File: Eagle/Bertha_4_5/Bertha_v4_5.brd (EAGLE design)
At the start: 100 x 83.6 mm, 132 parts, among them CON1 JACK_DC_BARREL, CON2 JACK_DC_BARREL, IC1 MCP1703DB, IC4 DRV8811, J1 RJ12RIGHTANGLE-I2C, J2 RJ12RIGHTANGLE-I2C, Q5 BSP75, Q6 BSP75, U1 HX711, U100 RN2483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

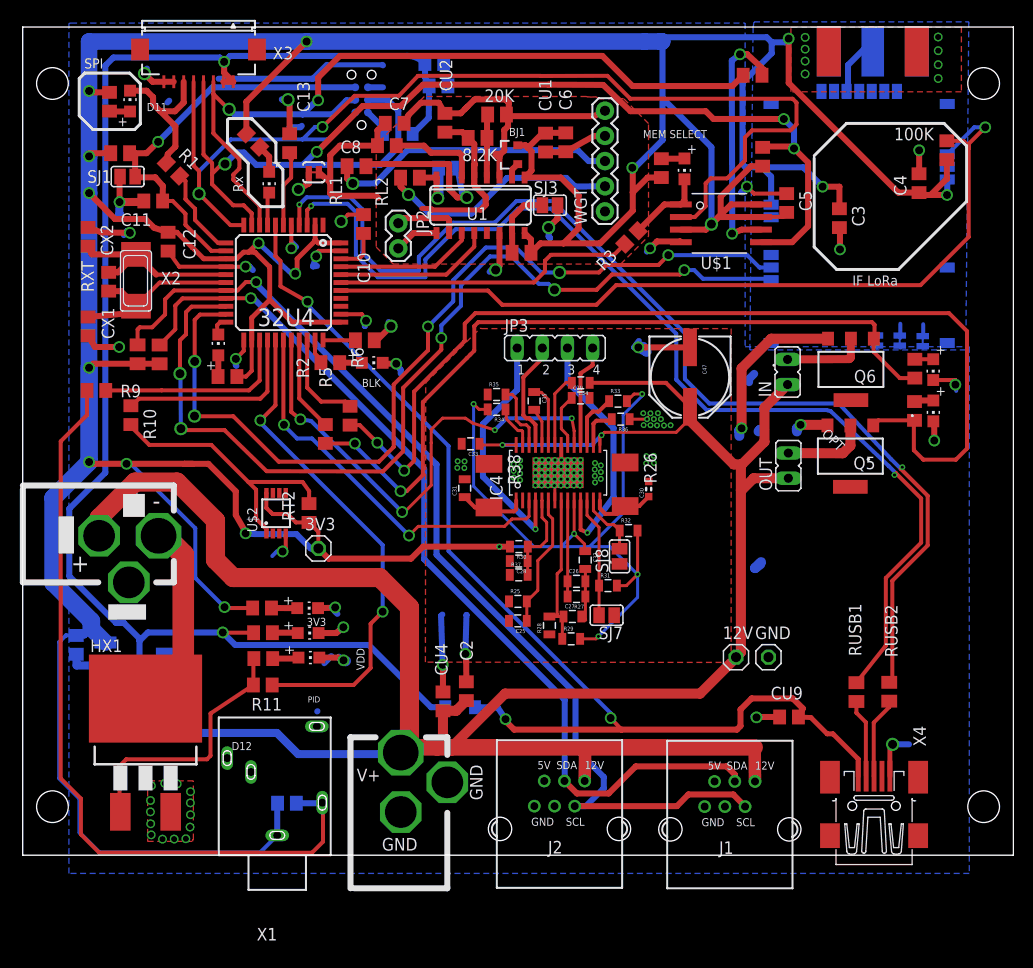
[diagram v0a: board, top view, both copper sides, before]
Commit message: correted PID diode, 4.5 finished, closes #72, ref #47
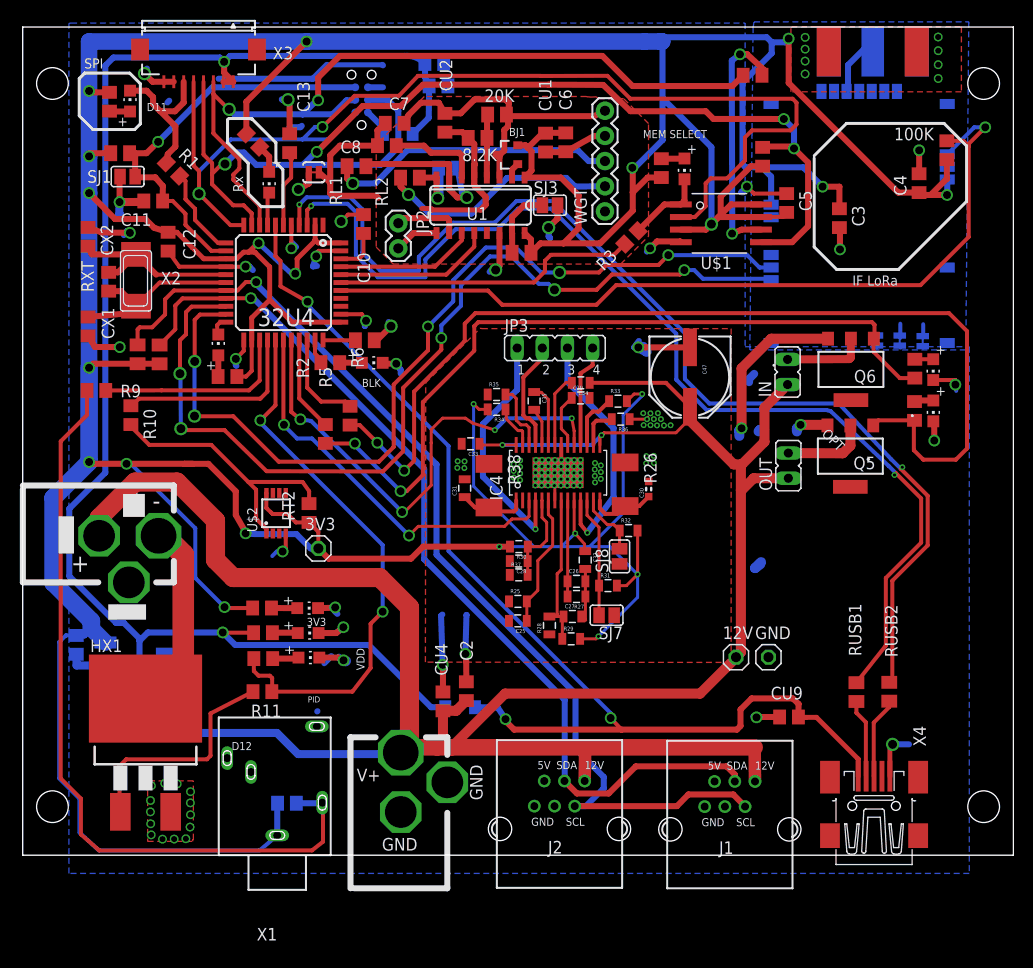
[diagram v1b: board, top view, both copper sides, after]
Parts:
- HX1: value IPB081N06L3GATMA1 -> 3v3 IGBT
- R28: value 0R -> Rlim
- moved R11 0.67 mm to (19.2, 14.6)
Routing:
- net D6*: track 50.0 -> 55.3 mm
- net N$6: track 26.4 -> 23.4 mm

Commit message: corrected powerFET labelling
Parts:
- HX1: value 3v3 IGBT -> <3V th / 10A
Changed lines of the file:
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@@
 </element>
 <element name="RK1" library="resistor" package="M0805" value="10K" x="8.82023125" y="48.6536625" smashed="yes" rot="R90"/>
-<element name="HX1" library="transistor-power" package="D2PACK" value="3v3 IGBT" x="7.39551875" y="11.3685"/>
+<element name="HX1" library="transistor-power" package="D2PACK" value="&lt;3V th / 10A" x="7.39551875" y="11.3685" smashed="yes">
+<attribute name="NAME" x="1.80751875" y="18.6075" size="1.27" layer="25"/>
+<attribute name="VALUE" x="3.2" y="7.980075" size="0.8128" layer="27"/>
+</element>
 <element name="R11" library="rcl" package="R0805" value="1K" x="19.194778125" y="14.6140875" smashed="yes" rot="R180">
 <attribute name="NAME" x="21.128021875" y="13.305246875" size="1.27" layer="25" rot="R180"/>

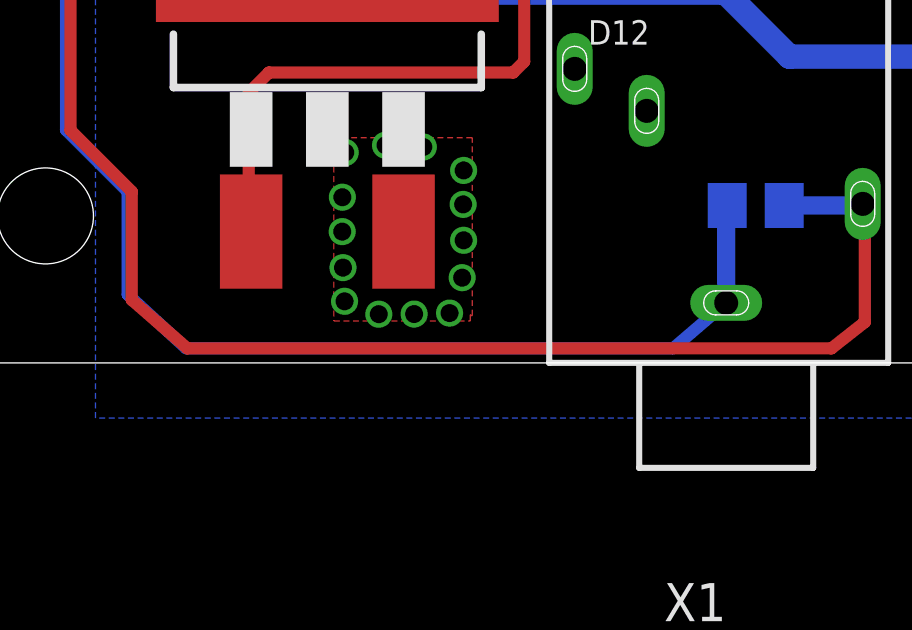
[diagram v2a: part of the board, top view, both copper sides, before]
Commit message: added protection resistor, closes #74
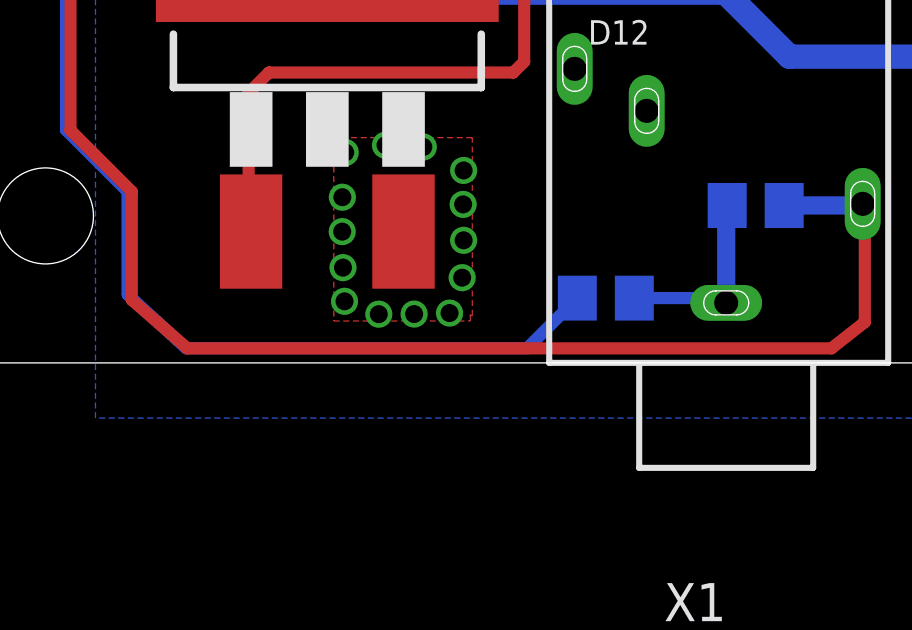
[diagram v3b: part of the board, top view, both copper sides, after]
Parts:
- added R4: 100, rcl:R0805
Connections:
- new net N$14: R4.1, RT1.1, X1.1
- net 3.3V: now also R4.2; no longer RT1.1, X1.1
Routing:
- net 3.3V: track 583.8 -> 575.7 mm
- net N$14: track 0.00 -> 6.39 mm
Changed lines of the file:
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@@
 </element>
 <element name="JP3" library="jumper" package="JP4" value="" x="48.7194" y="49.297871875"/>
+<element name="R4" library="rcl" package="R0805" value="100" x="16.678528125" y="0.2596125" smashed="yes" rot="MR0">
+<attribute name="NAME" x="17.313528125" y="1.5296125" size="1.27" layer="26" rot="MR0"/>
+<attribute name="VALUE" x="18.344796875" y="1.675675" size="1.27" layer="28" rot="MR0"/>
+</element>
 </elements>
 <signals>
@@
 <wire x1="47.592296875" y1="71.108425" x2="45.998725" y2="69.514853125" width="0.6096" layer="1"/>
 <contactref element="RT2" pad="1"/>
-<contactref element="RT1" pad="1"/>
 <contactref element="RK15" pad="1"/>
 <contactref element="RK16" pad="1"/>
@@
 <wire x1="58.084196875" y1="66.5093625" x2="56.578546875" y2="65.0037125" width="0.6096" layer="1"/>
 <wire x1="56.578546875" y1="65.0037125" x2="56.578546875" y2="63.1641625" width="0.6096" layer="1"/>
-<contactref element="X1" pad="1"/>
 <contactref element="U$2" pad="8"/>
 <wire x1="20.0952625" y1="32.67880625" x2="19.589753125" y2="33.144575" width="0.4064" layer="1"/>
@@
 <wire x1="22.625440625" y1="30.51745" x2="24.075609375" y2="29.06728125" width="0.6096" layer="16"/>
 <wire x1="24.075609375" y1="29.06728125" x2="24.84389375" y2="29.06728125" width="0.6096" layer="16"/>
-<wire x1="20.724303125" y1="3.347709375" x2="20.691253125" y2="3.314659375" width="0.6096" layer="16"/>
-<wire x1="20.691253125" y1="3.314659375" x2="20.691253125" y2="0.101475" width="0.6096" layer="16"/>
 <wire x1="-1.314634375" y1="5.865509375" x2="0.741525" y2="3.80935" width="0.4064" layer="16"/>
 <wire x1="0.741525" y1="3.80935" x2="0.741525" y2="0.3821125" width="0.4064" layer="16"/>
 <wire x1="0.741525" y1="0.3821125" x2="2.68780625" y2="-1.4120125" width="0.4064" layer="16"/>
-<wire x1="2.68780625" y1="-1.4120125" x2="18.924171875" y2="-1.4120125" width="0.4064" layer="16"/>
-<wire x1="18.924171875" y1="-1.4120125" x2="20.691253125" y2="0.101475" width="0.4064" layer="16"/>
 <wire x1="3.348034375" y1="19.565765625" x2="1.93053125" y2="20.98326875" width="1.6764" layer="16"/>
 <wire x1="0.77016875" y1="20.28466875" x2="1.23193125" y2="20.28466875" width="0.6096" layer="16"/>
@@
 <wire x1="50.7703" y1="30.58508125" x2="50.662753125" y2="30.692628125" width="0.3048" layer="1"/>
 <wire x1="50.662753125" y1="30.692628125" x2="50.662753125" y2="33.91315" width="0.3048" layer="1"/>
+<contactref element="R4" pad="2"/>
+<wire x1="2.68780625" y1="-1.4120125" x2="14.056903125" y2="-1.4120125" width="0.4064" layer="16"/>
+<wire x1="14.056903125" y1="-1.4120125" x2="15.728528125" y2="0.2596125" width="0.4064" layer="16"/>
 </signal>
 <signal name="SDA">
@@
 <wire x1="51.3184125" y1="31.49996875" x2="51.312753125" y2="33.91315" width="0.4064" layer="1"/>
 </signal>
+<signal name="N$14" class="1">
+<contactref element="RT1" pad="1"/>
+<contactref element="X1" pad="1"/>
+<wire x1="20.724303125" y1="3.347709375" x2="20.691253125" y2="3.314659375" width="0.6096" layer="16"/>
+<wire x1="20.691253125" y1="3.314659375" x2="20.691253125" y2="0.101475" width="0.6096" layer="16"/>
+<contactref element="R4" pad="1"/>
+<wire x1="17.628528125" y1="0.2596125" x2="20.533115625" y2="0.2596125" width="0.4064" layer="16"/>
+<wire x1="20.533115625" y1="0.2596125" x2="20.691253125" y2="0.101475" width="0.4064" layer="16"/>
+</signal>
 </signals>

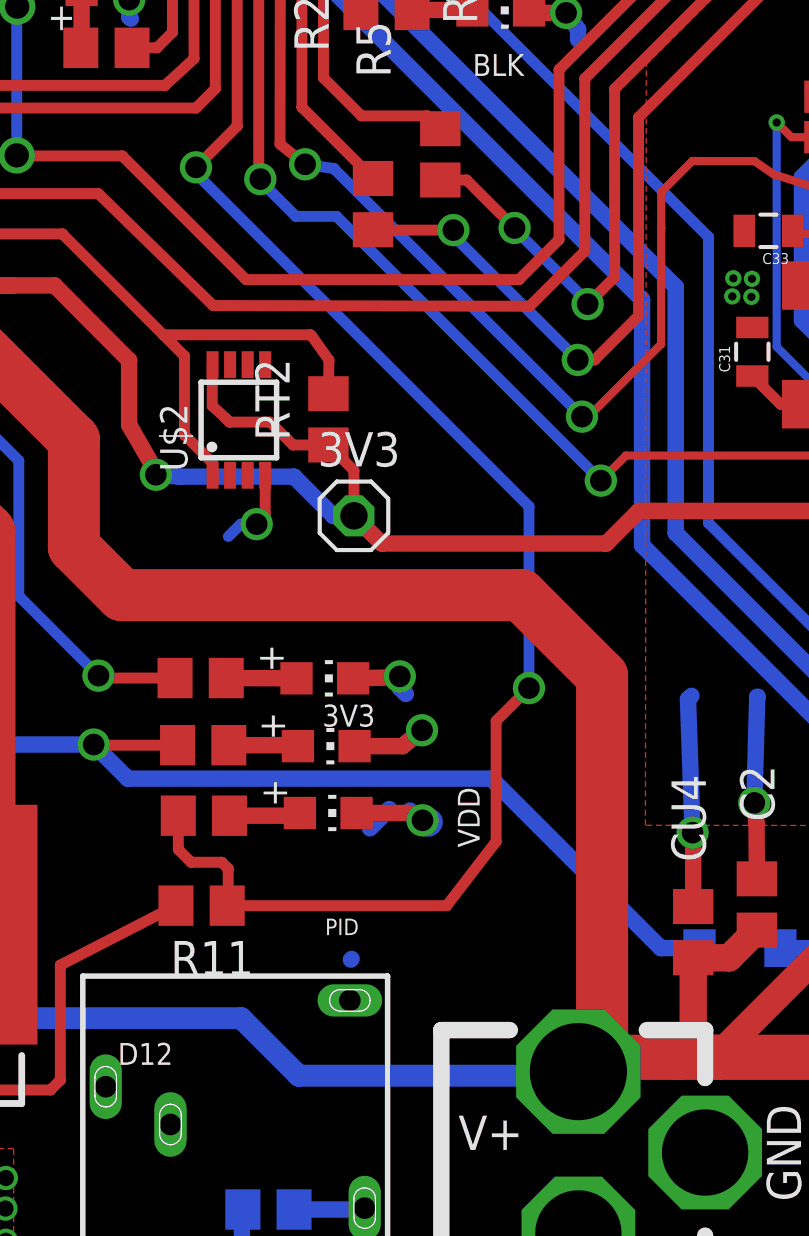
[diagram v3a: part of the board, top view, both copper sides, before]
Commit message: added high side power switch with 5.6V zener on V4.5, drafted hack modif on 4.4, To be tested
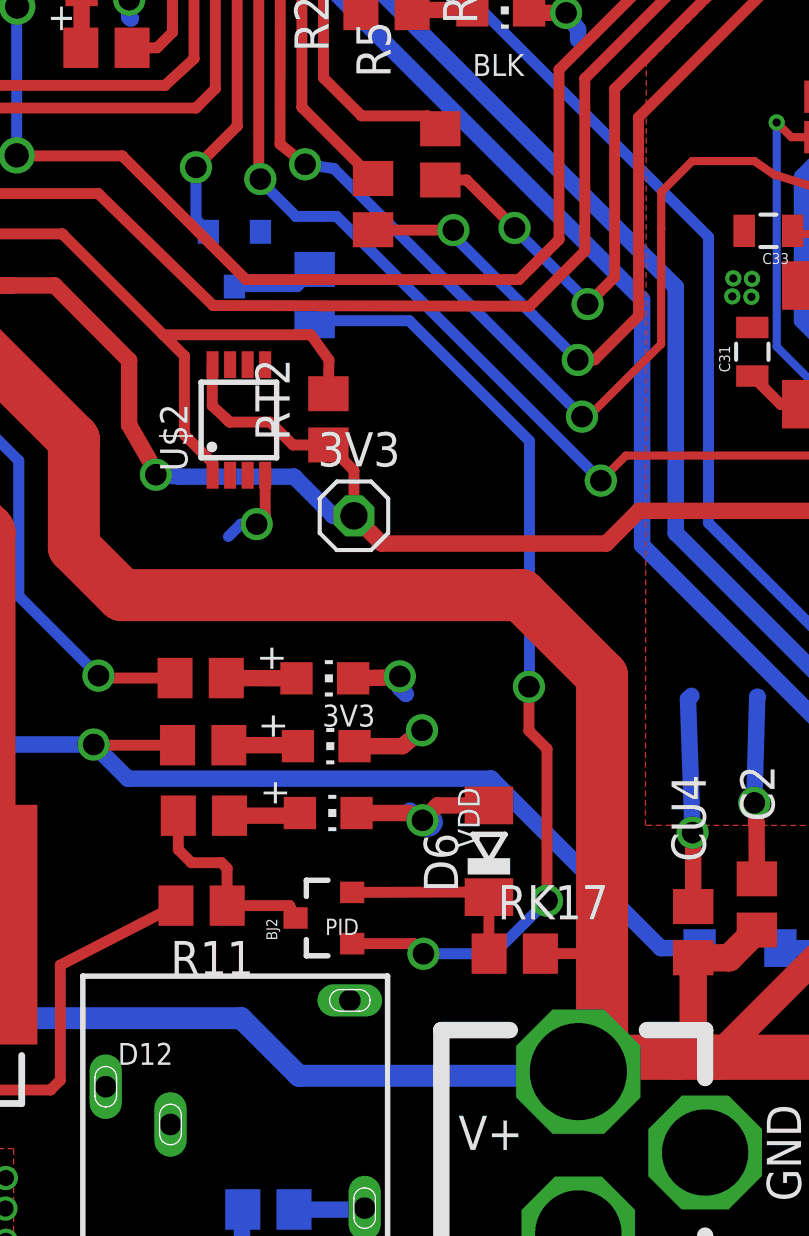
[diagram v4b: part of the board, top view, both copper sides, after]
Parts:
- added BJ2: MMBT4403, SparkFun-DiscreteSemi:SOT23-3
- added D6: 5.6V ZNR, diode:SOD80C
- added RK17, RK20: 1k, rcl:R0805
- added T1: 2n7002, zetex:SOT-23
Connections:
- new net N$16: BJ2.3, R11.1, RK14.2
- new net N$19: BJ2.2, D6.C, RK17.1
- new net N$31: BJ2.1, RK20.1
- new net N$32: RK20.2, T1.1
- net +12V: now also RK17.2
- net D6*: now also T1.3; no longer R11.1, RK14.2
- net GND: now also D6.A, T1.2
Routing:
- net D6*: track 55.3 -> 11.3 mm, vias 2 -> 1
- net N$31: track 0.00 -> 35.3 mm, vias 0 -> 3
- net N$16: track 0.00 -> 7.56 mm
- net N$19: track 0.00 -> 7.31 mm
- net N$32: track 0.00 -> 3.24 mm
- net +12V: track 244.7 -> 247.0 mm
- net GND: track 191.7 -> 193.3 mm

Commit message: pretty sch for 4.5
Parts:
- RK14: value 1k -> 10k
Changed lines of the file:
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@@
 <attribute name="VALUE" x="81.084303125" y="39.705115625" size="0.8128" layer="27" rot="R180"/>
 </element>
-<element name="RK14" library="rcl" package="R0805" value="1k" x="19.28185625" y="17.94956875" smashed="yes" rot="R180">
+<element name="RK14" library="rcl" package="R0805" value="10k" x="19.28185625" y="17.94956875" smashed="yes" rot="R180">
 <attribute name="VALUE" x="16.145696875" y="18.65589375" size="0.8128" layer="27" rot="R270"/>
 </element>

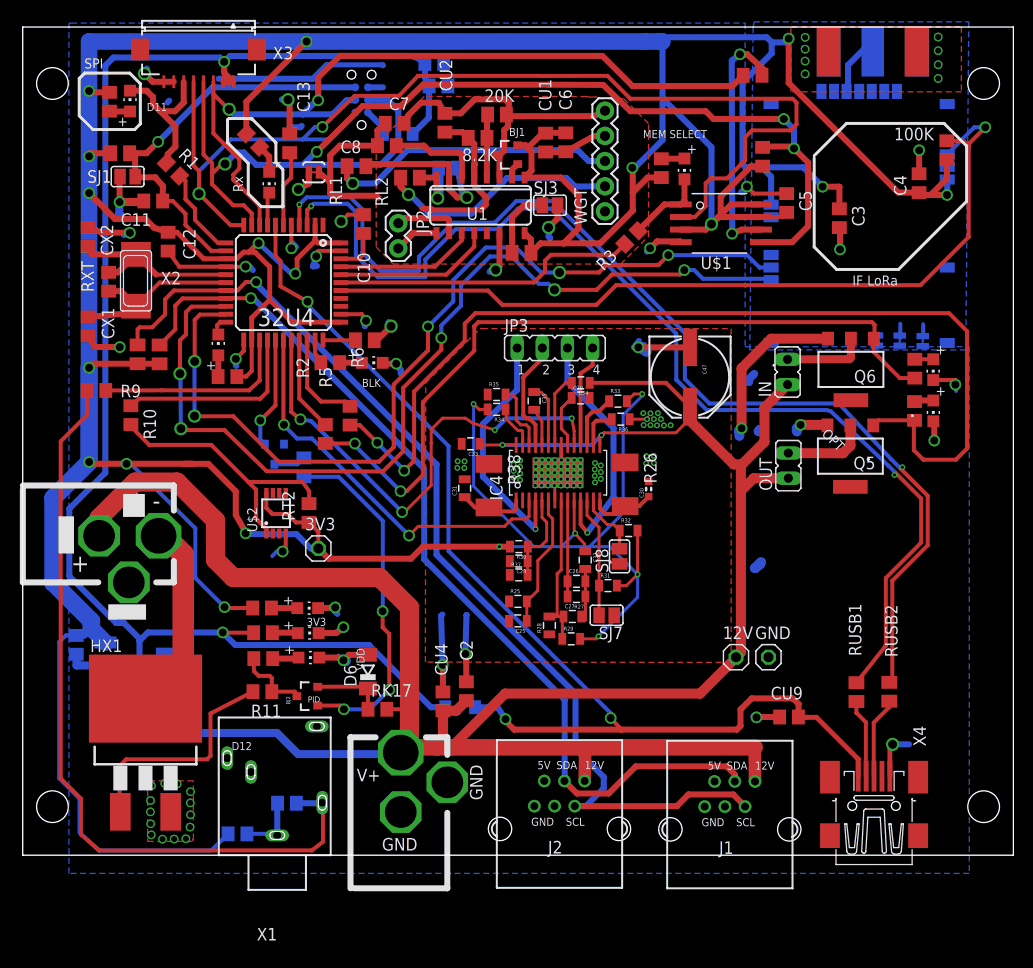
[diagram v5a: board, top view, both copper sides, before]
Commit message: JTAG on top
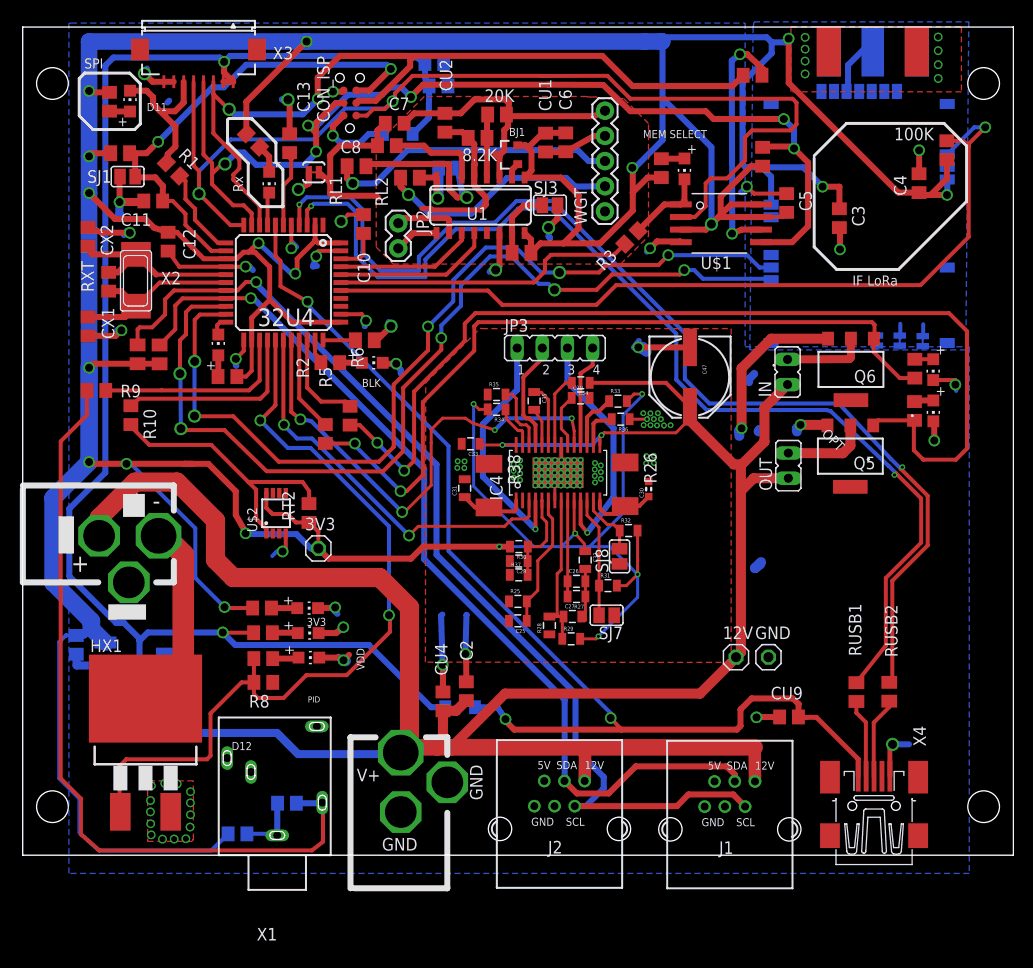
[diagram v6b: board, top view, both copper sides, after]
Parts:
- removed BJ2: MMBT4403, SparkFun-DiscreteSemi:SOT23-3
- removed D6: 5.6V ZNR, diode:SOD80C
- removed R11: 1K, rcl:R0805
- removed RK17, RK20: 1k, rcl:R0805
- removed T1: 2n7002, zetex:SOT-23
- added R8: 1k, rcl:R0805
- moved CON_ISP 1.22 mm to (28.0, 71.5), flipped to the top
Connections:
- removed net N$16: BJ2.3, R11.1, RK14.2
- removed net N$19: BJ2.2, D6.C, RK17.1
- removed net N$31: BJ2.1, RK20.1
- removed net N$32: RK20.2, T1.1
- removed net N$6: HX1.1, R11.2
- net +12V: no longer RK17.2
- net D6*: now also HX1.1, R8.2, RK14.2; no longer T1.3
- net GND: no longer D6.A, T1.2
- net N$26: now also R8.1
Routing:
- net D6*: track 11.3 -> 81.3 mm, vias 1 -> 2
- net N$31: track 35.3 -> 0.00 mm, vias 3 -> 0
- net N$6: track 23.4 -> 0.00 mm
- net GND: track 193.3 -> 172.6 mm, vias 118 -> 119
- net MOSI: track 119.1 -> 109.8 mm, vias 4 -> 6
- net RESET: track 42.3 -> 51.6 mm, vias 1 -> 2
- net N$16: track 7.56 -> 0.00 mm
- net N$19: track 7.31 -> 0.00 mm
- net ISP+5V: track 2.80 -> 8.85 mm, vias 0 -> 1
- net N$32: track 3.24 -> 0.00 mm
- net SCK: track 82.7 -> 84.9 mm
- net +12V: track 247.0 -> 244.9 mm
- net MISO: track 112.0 -> 110.1 mm
- net N$5: track 31.7 -> 30.5 mm

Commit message: change resistor select flash to 1k
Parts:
- RK19: value 10k -> 1k
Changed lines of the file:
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@@
 <?xml version="1.0" encoding="utf-8"?>
 <!DOCTYPE eagle SYSTEM "eagle.dtd">
-<eagle version="8.0.1">
+<eagle version="7.7.0">
 <drawing>
 <settings>
@@
 <attribute name="VALUE" x="17.702921875" y="67.895596875" size="0.8128" layer="27" rot="R270"/>
 </element>
-<element name="RK19" library="rcl" package="R0805" value="10k" x="59.464703125" y="67.4593625" smashed="yes" rot="R90">
+<element name="RK19" library="rcl" package="R0805" value="1k" x="59.464703125" y="67.4593625" smashed="yes" rot="R90">
 <attribute name="VALUE" x="59.802565625" y="70.19068125" size="0.8128" layer="27" rot="R90"/>
 </element>
